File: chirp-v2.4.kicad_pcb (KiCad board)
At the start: 2 copper layers, 140.8 x 16 mm, 20 parts, among them IC1 TINY24/44/84-SSU, SW1 SPST_TACTFSMJSMA

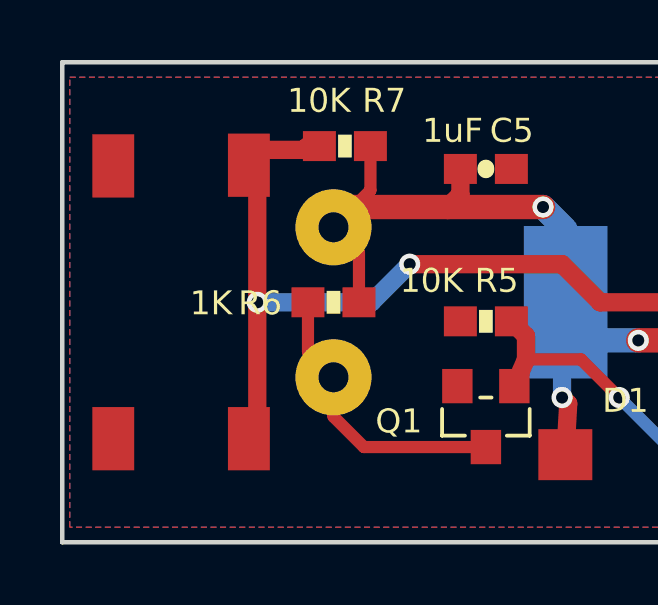
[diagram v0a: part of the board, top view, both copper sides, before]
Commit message: Add manufacturing set, tune up the silkscreen on the board
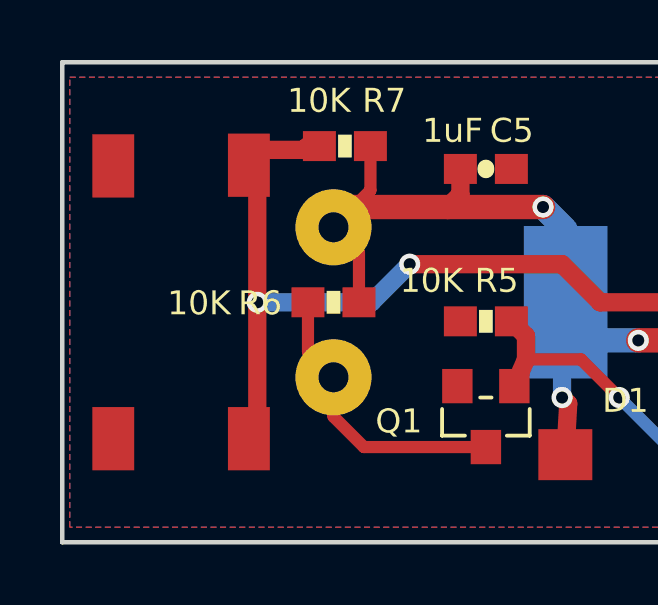
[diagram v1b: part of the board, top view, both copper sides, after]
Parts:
- R6: value 1K -> 10K
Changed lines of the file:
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@@
-(kicad_pcb (version 4) (host pcbnew 0.201510241816+6277~30~ubuntu14.04.1-product)
+(kicad_pcb (version 4) (host pcbnew 0.201602211417+6576~42~ubuntu14.04.1-product)
   (general
     (links 40)
     (no_connects 0)
-    (area 77.5687 96.8387 219.325001 114.4824)
+    (area 78.424999 96.924999 219.325001 113.075001)
     (thickness 1.6)
     (drawings 16)
@@
   (layers
     (0 Top signal)
-    (31 Bottom signal)
+    (31 Bottom signal hide)
     (32 B.Adhes user)
     (33 F.Adhes user)
@@
     (visible_elements FFFFFF7F)
     (pcbplotparams
-      (layerselection 0x00030_80000001)
+      (layerselection 0x00030_ffffffff)
       (usegerberextensions false)
       (excludeedgelayer true)
@@
       (hpglpenspeed 20)
       (hpglpendiameter 15)
-      (hpglpenoverlay 2)
       (psnegative false)
       (psa4output false)
@@
       (padsonsilk false)
       (subtractmaskfromsilk false)
-      (outputformat 1)
+      (outputformat 5)
       (mirror false)
-      (drillshape 1)
+      (drillshape 0)
       (scaleselection 1)
-      (outputdirectory ""))
+      (outputdirectory mfg/))
   )
   (net 0 "")
@@
     (add_net V_CAP)
   )
+  (module FSMJSMA (layer Top)
+    (at 82.4611 105.0011 90)
+    (attr smd)
+    (fp_text reference SW1 (at 0 5 90) (layer F.SilkS) hide
+      (effects (font (size 0.8 0.8) (thickness 0.12)))
+    )
+    (fp_text value SPST_TACTFSMJSMA (at 0 -4 90) (layer F.SilkS) hide
+      (effects (font (size 0.8 0.8) (thickness 0.12)))
+    )
+    (fp_circle (center 0 0) (end 1.5 0) (layer F.CrtYd) (width 0.15))
+    (fp_line (start 4.5 2.5) (end 3 2.5) (layer F.CrtYd) (width 0.15))
+    (fp_line (start 4.5 2) (end 4.5 2.5) (layer F.CrtYd) (width 0.15))
+    (fp_line (start 3 2) (end 4.5 2) (layer F.CrtYd) (width 0.15))
+    (fp_line (start 4.5 -2) (end 3 -2) (layer F.CrtYd) (width 0.15))
+    (fp_line (start 4.5 -2.5) (end 4.5 -2) (layer F.CrtYd) (width 0.15))
+    (fp_line (start 3 -2.5) (end 4.5 -2.5) (layer F.CrtYd) (width 0.15))
+    (fp_line (start -4.5 2.5) (end -3 2.5) (layer F.CrtYd) (width 0.15))
+    (fp_line (start -4.5 2) (end -4.5 2.5) (layer F.CrtYd) (width 0.15))
+    (fp_line (start -3 2) (end -4.5 2) (layer F.CrtYd) (width 0.15))
+    (fp_line (start -4.5 -2) (end -3 -2) (layer F.CrtYd) (width 0.15))
+    (fp_line (start -4.5 -2.5) (end -4.5 -2) (layer F.CrtYd) (width 0.15))
+    (fp_line (start -3 -2.5) (end -4.5 -2.5) (layer F.CrtYd) (width 0.15))
+    (fp_line (start -3 3) (end -3 -3) (layer F.CrtYd) (width 0.15))
+    (fp_line (start 3 3) (end -3 3) (layer F.CrtYd) (width 0.15))
+    (fp_line (start 3 -3) (end 3 3) (layer F.CrtYd) (width 0.15))
+    (fp_line (start -3 -3) (end 3 -3) (layer F.CrtYd) (width 0.15))
+    (pad B smd rect (at -4.5466 -2.2606 90) (size 2.1082 1.397) (layers Top F.Paste F.Mask)
+      (net 2 GND))
+    (pad B' smd rect (at 4.5466 -2.2606 90) (size 2.1082 1.397) (layers Top F.Paste F.Mask)
+      (net 2 GND))
+    (pad A' smd rect (at 4.5684 2.2606 90) (size 2.1082 1.397) (layers Top F.Paste F.Mask)
+      (net 3 RESET))
+    (pad A smd rect (at -4.5466 2.2606 90) (size 2.1082 1.397) (layers Top F.Paste F.Mask)
+      (net 3 RESET))
+  )
   (module SOD-523 (layer Top)
     (at 120.5611 101.1911 90)
     (descr "SOD-523 (0.8x1.2mm) <p>Source: http://www.rohm.com/products/databook/di/pdf/rb751s-40.pdf</p>")
+    (attr smd)
     (fp_text reference D2 (at -0.5589 -2.8111 180) (layer F.SilkS)
       (effects (font (size 0.8 0.8) (thickness 0.12)) (justify left bottom))
@@
     (at 107.2261 110.0811 270)
     (descr "<b>CHIPLED</b><p> Source: http://www.osram.convergy.de/ ... LG_R971.pdf")
+    (attr smd)
     (fp_text reference LED1 (at 1.9189 1.2261 360) (layer F.SilkS)
       (effects (font (size 0.8 0.8) (thickness 0.12)) (justify left bottom))
@@
     (at 97.3201 110.0811)
     (descr <b>DIODE</b>)
+    (attr smd)
     (fp_text reference D1 (at -0.8201 -1.3311) (layer F.SilkS)
       (effects (font (size 0.8 0.8) (thickness 0.12)) (justify left bottom))
@@
     (at 112.9411 105.0011)
     (descr "<b>Small Outline Package</b>")
+    (attr smd)
     (fp_text reference IC1 (at -4.5085 2.032 90) (layer F.SilkS)
       (effects (font (size 0.8 0.8) (thickness 0.12)) (justify left bottom))
@@
   (module PS12 (layer Bottom)
     (at 87.5411 105.0011 270)
+    (attr smd)
     (fp_text reference SP1 (at -2.54 6.35 270) (layer B.SilkS) hide
       (effects (font (size 0.8 0.8) (thickness 0.12)) (justify left bottom mirror))
@@
     (pad P$2 thru_hole circle (at 2.5 0 270) (size 2.54 2.54) (drill 1) (layers *.Cu *.Mask)
       (net 8 N$1))
-  )
-  (module FSMJSMA (layer Top)
-    (at 82.4611 105.0011 90)
-    (fp_text reference SW1 (at 0 5 90) (layer F.SilkS) hide
-      (effects (font (size 0.8 0.8) (thickness 0.12)))
-    )
-    (fp_text value SPST_TACTFSMJSMA (at 0 -4 90) (layer F.SilkS) hide
-      (effects (font (size 0.8 0.8) (thickness 0.12)))
-    )
-    (pad B smd rect (at -4.5466 -2.2606 90) (size 2.1082 1.397) (layers Top F.Paste F.Mask)
-      (net 2 GND))
-    (pad B' smd rect (at 4.5466 -2.2606 90) (size 2.1082 1.397) (layers Top F.Paste F.Mask)
-      (net 2 GND))
-    (pad A' smd rect (at 4.5684 2.2606 90) (size 2.1082 1.397) (layers Top F.Paste F.Mask)
-      (net 3 RESET))
-    (pad A smd rect (at -4.5466 2.2606 90) (size 2.1082 1.397) (layers Top F.Paste F.Mask)
-      (net 3 RESET))
   )
   (module BAT-HLD-001 (layer Bottom)
@@
     (at 92.6211 108.8111 180)
     (descr <b>SOT23</b>)
+    (attr smd)
     (fp_text reference Q1 (at 2.1211 0.3111 180) (layer F.SilkS)
       (effects (font (size 0.8 0.8) (thickness 0.12)) (justify right top))
@@
   (module 0603-RES (layer Top)
     (at 92.6211 105.6361)
+    (attr smd)
     (fp_text reference R5 (at -0.3711 -0.8861) (layer F.SilkS)
       (effects (font (size 0.8 0.8) (thickness 0.12)) (justify left bottom))
@@
   (module 0603-RES (layer Top)
     (at 87.5411 105.0011)
+    (attr smd)
     (fp_text reference R6 (at -3.175 0.4989) (layer F.SilkS)
       (effects (font (size 0.8 0.8) (thickness 0.12)) (justify left bottom))
     )
-    (fp_text value 1K (at -4.7911 0.4989) (layer F.SilkS)
+    (fp_text value 10K (at -5.5411 0.4989) (layer F.SilkS)
       (effects (font (size 0.8 0.8) (thickness 0.12)) (justify left bottom))
     )
@@
   (module 0603-CAP (layer Top)
     (at 107.2261 107.5411 180)
+    (attr smd)
     (fp_text reference C2 (at 1.7261 0.2911 360) (layer F.SilkS)
       (effects (font (size 0.8 0.8) (thickness 0.12)) (justify right top))
@@
   (module 0603-RES (layer Top)
     (at 87.9221 99.7941)
+    (attr smd)
     (fp_text reference R7 (at 0.5779 -1.0441) (layer F.SilkS)
       (effects (font (size 0.8 0.8) (thickness 0.12)) (justify left bottom))
@@
   (module 0603-CAP (layer Top)
     (at 105.3211 103.7311 180)
+    (attr smd)
     (fp_text reference C3 (at 3.3211 -0.2689 360) (layer F.SilkS)
       (effects (font (size 0.8 0.8) (thickness 0.12)) (justify left bottom))
@@
   (module 0603-RES (layer Top)
     (at 120.5611 104.3661 180)
+    (attr smd)
     (fp_text reference R1 (at -1.6889 1.6161 180) (layer F.SilkS)
       (effects (font (size 0.8 0.8) (thickness 0.12)) (justify right top))
@@
   (module 0603-CAP (layer Top)
     (at 120.5611 99.2861)
+    (attr smd)
     (fp_text reference C4 (at 0.4389 -0.7861) (layer F.SilkS)
       (effects (font (size 0.8 0.8) (thickness 0.12)) (justify left bottom))
@@
   (module 0603-RES (layer Top)
     (at 110.4011 99.2861 180)
+    (attr smd)
     (fp_text reference R2 (at 2.1511 0.2861 180) (layer F.SilkS)
       (effects (font (size 0.8 0.8) (thickness 0.12)) (justify right top))
@@
   (module 0603-RES (layer Top)
     (at 103.0351 110.0811 180)
+    (attr smd)
     (fp_text reference R3 (at -1.7149 -1.4189 180) (layer F.SilkS)
       (effects (font (size 0.8 0.8) (thickness 0.12)) (justify right top))
@@
   (module 0603-CAP (layer Top)
     (at 92.6211 100.5561)
+    (attr smd)
     (fp_text reference C5 (at 0.1289 -0.8061) (layer F.SilkS)
       (effects (font (size 0.8 0.8) (thickness 0.12)) (justify left bottom))

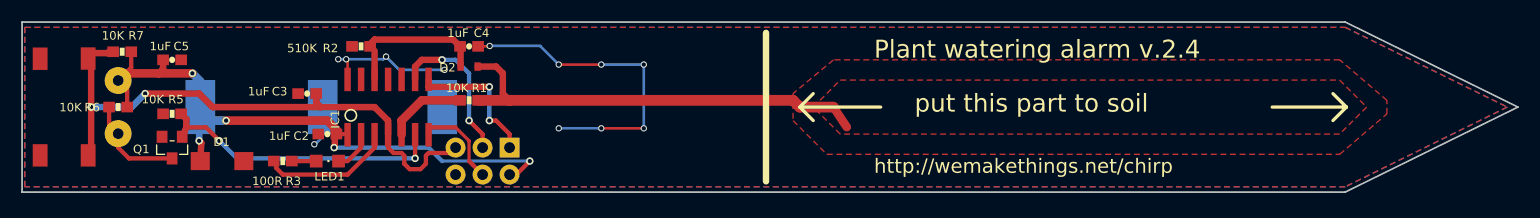
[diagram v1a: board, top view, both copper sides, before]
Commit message: Add hardware changes - add U1 LDO regulator, connect ISP VCC to battery, update cap values, update footprints, update routing, update battery footprint
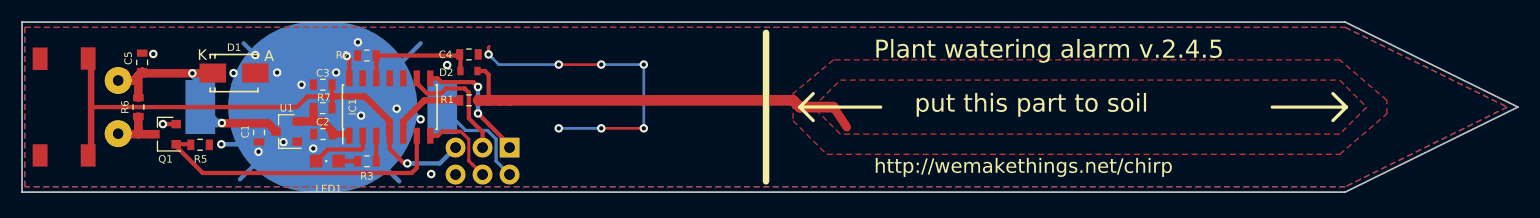
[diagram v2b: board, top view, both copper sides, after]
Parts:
- added C1: 1u, Capacitor_SMD:C_0603_1608Metric, F.Cu at (100.8, 107.4)
- added U1: MCP1700-2502E_SOT23, TO_SOT_Packages_SMD:SOT-23, F.Cu at (103.4, 107.3)
- BT1: renamed from B1; value (none) -> Battery_Cell
- C2, C3, C5: value 1uF -> 1u; footprint 0603-CAP -> Capacitor_SMD:C_0603_1608Metric
- C4: value 1uF -> 1n; footprint 0603-CAP -> Capacitor_SMD:C_0603_1608Metric
- D1: value (none) -> D; footprint DO214AC -> Diodes_SMD:Diode-SMA_Standard
- IC1: footprint SOIC14 -> Housings_SOIC:SOIC-14_3.9x8.7mm_Pitch1.27mm
- LED1: value (none) -> LEDCHIPLED_0805
- Q1: value (none) -> MOSFET-N-SOT23; footprint SOT23 -> TO_SOT_Packages_SMD:SOT-23
- R1, R3, R5, R7: footprint 0603-RES -> Resistors_SMD:R_0603_1608Metric
- R2: value 510K -> 1M; footprint 0603-RES -> Resistors_SMD:R_0603_1608Metric
- R6: value 10K -> 1K; footprint 0603-RES -> Resistors_SMD:R_0603_1608Metric
- moved R7 19.6 mm to (106.8, 105.1), turned to 180 degrees
- moved G*** 10.1 mm to (157.1, 105.0)
- moved D1 8.36 mm to (98.5, 101.8), turned to 180 degrees
- moved R3 7.91 mm to (111.0, 110.1), turned to 0 degrees
- moved R5 3.92 mm to (95.2, 108.5), turned to 180 degrees
- moved C5 2.83 mm to (89.8, 100.8), turned to 90 degrees
- moved R6 1.91 mm to (89.5, 105.0), turned to 90 degrees
- moved C3 1.70 mm to (106.8, 102.9)
- moved Q1 1.41 mm to (92.0, 107.5)
- moved R2 1.02 mm to (111.0, 100.2)
- moved C4 0.76 mm to (120.5, 100.0)
- moved D2 0.41 mm to (120.5, 101.6)
- moved C2 0.40 mm to (106.8, 107.5)
- moved IC1 0.16 mm to (113.1, 105.0), turned to 90 degrees
- turned LED1 to 90 degrees
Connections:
- net BUZZER renamed Net-(IC1-Pad6)
- net CAPACITANCE_V renamed /CAPACITANCE_V
- net CLK_OUT renamed /CLK_OUT
- net LED_A renamed /LED_A
- net LED_K renamed /LED_K
- net MISO renamed /MISO
- net MOSI renamed /MOSI
- net RESET renamed /RESET
- net SCK renamed /SCK
- net V_CAP renamed /SENSE
- BT1 pad 3: (no net) -> VCC
- C2 pad 1: VCC -> +2V5
- IC1 pad 1: VCC -> +2V5
- IC1 pad 10: (no net) -> Net-(IC1-Pad10)
- IC1 pad 11: (no net) -> Net-(IC1-Pad11)
- IC1 pad 13: (no net) -> Net-(IC1-Pad13)
- R7 pad 2: VCC -> +2V5
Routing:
- net GND: track 46.8 -> 88.3 mm, vias 12 -> 25
- net VCC: track 61.5 -> 36.2 mm, vias 5 -> 2
- net /LED_A: track 12.5 -> 2.40 mm
- net +2V5: track 0.00 -> 6.51 mm
- net Net-(Q1-Pad3): track 9.66 -> 4.95 mm
- net /RESET: track 54.7 -> 59.1 mm, vias 2 -> 1
- net /SCK: track 14.6 -> 11.8 mm, vias 2 -> 0
- net /CAPACITANCE_V: track 14.3 -> 11.6 mm
- net /LED_K: track 3.86 -> 6.04 mm
- net /SENSE: track 41.4 -> 39.6 mm
- net /MISO: track 13.4 -> 11.8 mm
- net Net-(IC1-Pad6): track 27.4 -> 28.6 mm, vias 2 -> 0
- net /MOSI: track 8.67 -> 7.84 mm
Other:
- net class Default: via_dia 0.6 -> 0.8
- board text added: "Plant watering alarm v.2.4.5"
- board text removed: "Plant watering alarm v.2.4"
